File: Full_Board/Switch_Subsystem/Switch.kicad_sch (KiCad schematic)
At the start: 7 parts, among them U7 JS102011SCQN, U8 UCLAMP3301H.TCT

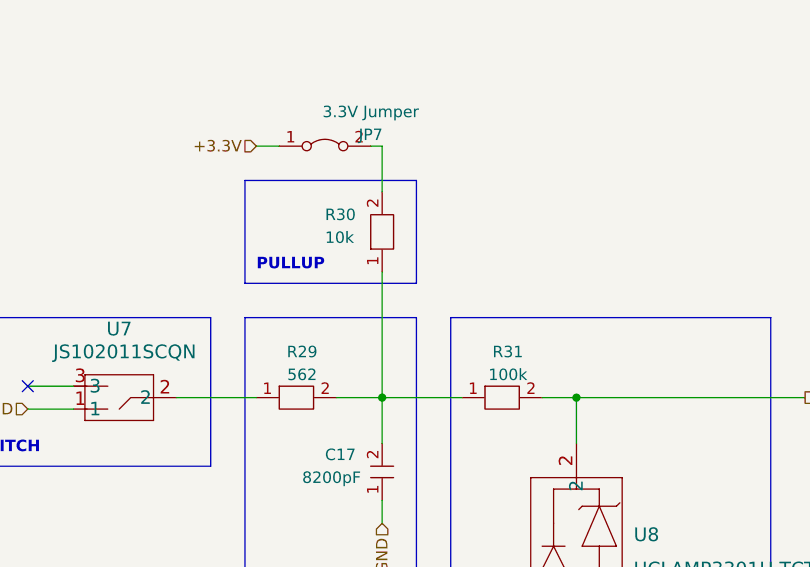
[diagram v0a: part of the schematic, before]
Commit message: Replace small resistors/capacitors with through-hole; fix DRC aside from electromagnet and MUXes
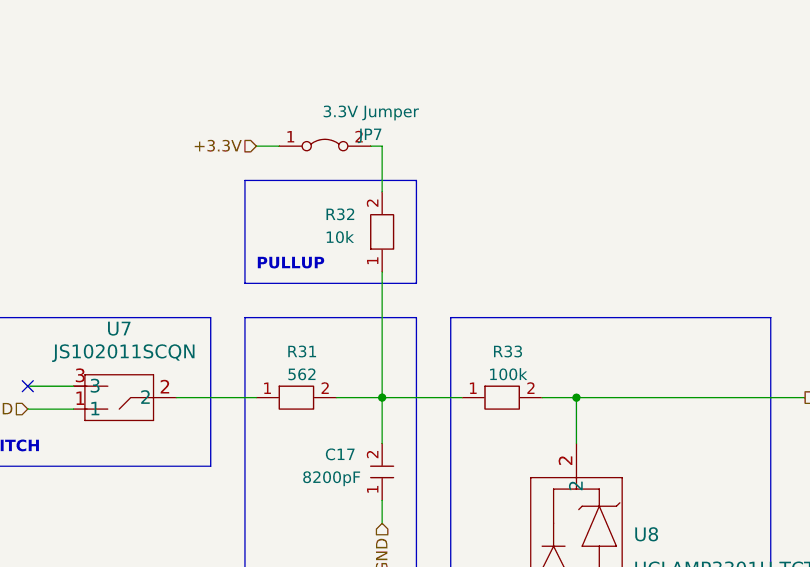
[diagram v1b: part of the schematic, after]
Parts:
- renumbered R29 to R31, R30 to R32, R31 to R33
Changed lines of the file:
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@@
   (symbol (lib_id "RMCF1206FT10K0:10k") (at 137.16 80.01 90) (unit 1)
     (in_bom yes) (on_board yes)
-    (property "Reference" "R30" (id 0) (at 130.81 73.66 90)
+    (property "Reference" "R32" (id 0) (at 130.81 73.66 90)
       (effects (font (size 1.27 1.27)) (justify right))
     )
@@
   (symbol (lib_id "CR0402-FX-5620GLF:CR0402-FX-5620GLF") (at 123.19 93.98 0) (unit 1)
     (in_bom yes) (on_board yes)
-    (property "Reference" "R29" (id 0) (at 128.27 88.9 0))
+    (property "Reference" "R31" (id 0) (at 128.27 88.9 0))
     (property "Value" "562" (id 1) (at 128.27 91.44 0))
     (property "Footprint" "CR0402-FX-5620GLF:RESC1005X40N" (id 2) (at 137.16 92.71 0)
@@
   (symbol (lib_id "RCV2512100KFKEGAT:RCV2512100KFKEGAT") (at 146.05 93.98 0) (unit 1)
     (in_bom yes) (on_board yes)
-    (property "Reference" "R31" (id 0) (at 151.13 88.9 0))
+    (property "Reference" "R33" (id 0) (at 151.13 88.9 0))
     (property "Value" "100k" (id 1) (at 151.13 91.44 0))
     (property "Footprint" "RCV2512100KFKEGAT:RESC6332X70N" (id 2) (at 160.02 92.71 0)
